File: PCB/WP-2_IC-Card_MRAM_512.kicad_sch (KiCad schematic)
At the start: 18 parts, among them J1 SMS-138-01-G-S, SW1 CUS-14TB, U1 MR2A08xxYSxxx, U2 16827, U3 8T245, U4 MIC5317-3.3YD5, U5 2G32

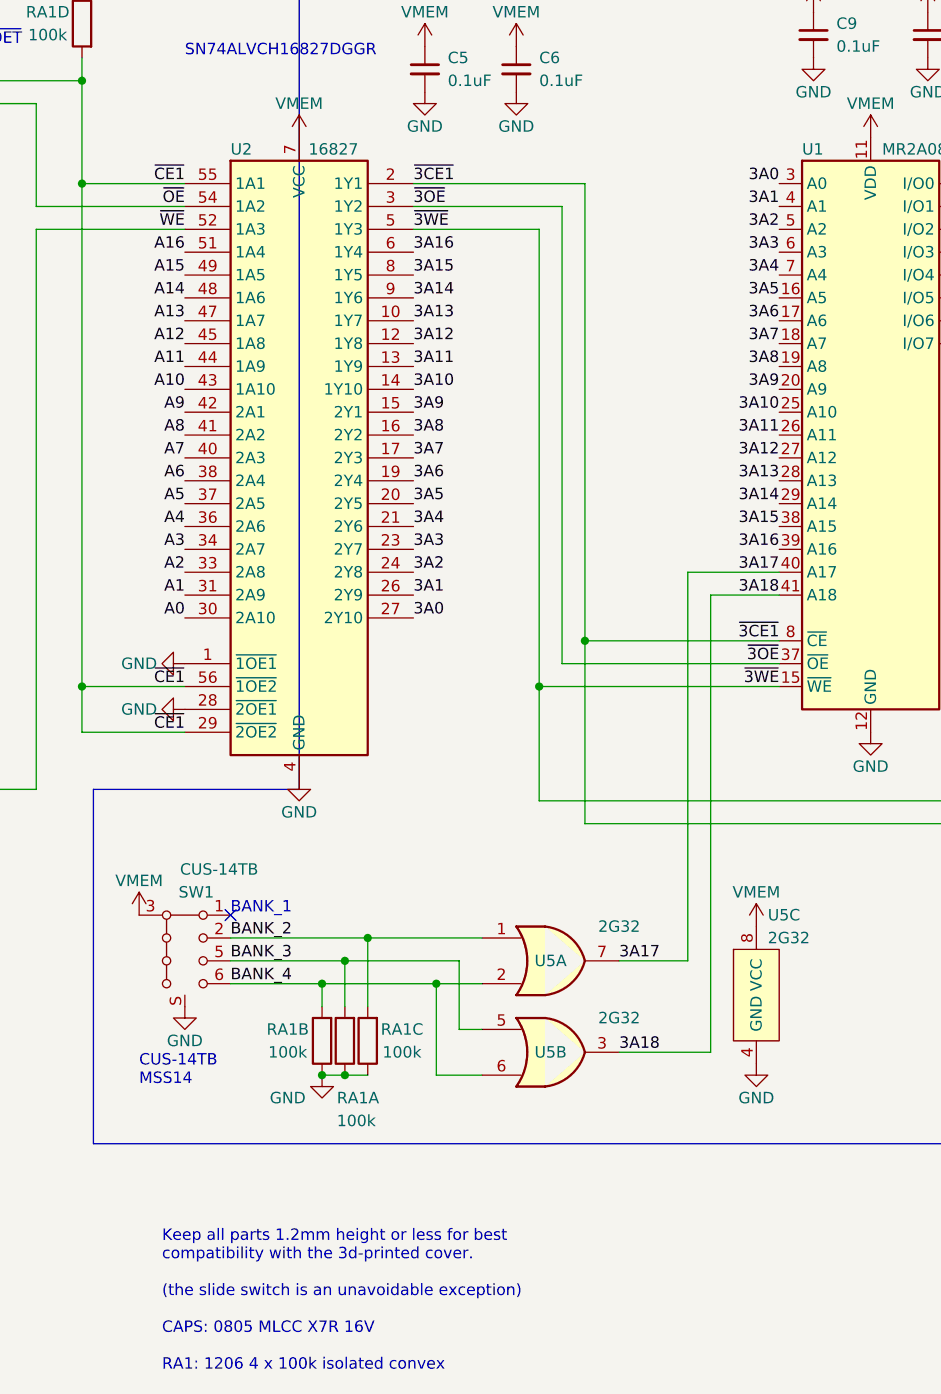
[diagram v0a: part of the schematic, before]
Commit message: mram 512 level-shift parts, battery backed ram top cover
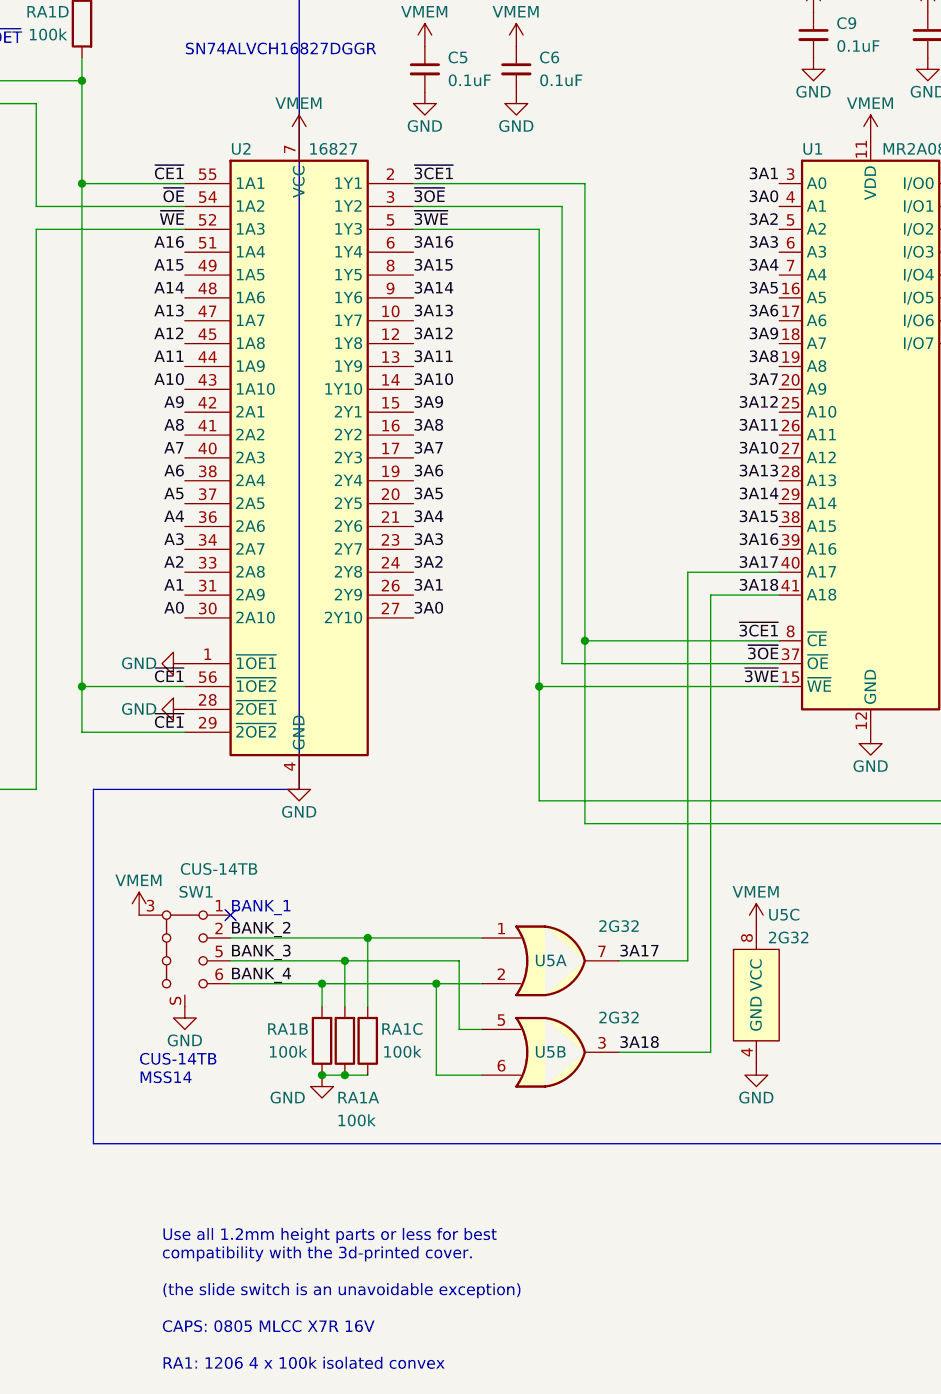
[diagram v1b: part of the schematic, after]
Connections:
- net 3A0: now also U1.4 (A1); no longer U1.3 (A0)
- net 3A1: now also U1.3 (A0); no longer U1.4 (A1)
- net 3A10: now also U1.27 (A12); no longer U1.25 (A10)
- net 3A12: now also U1.25 (A10); no longer U1.27 (A12)
- net 3A7: now also U1.20 (A9); no longer U1.18 (A7)
- net 3A9: now also U1.18 (A7); no longer U1.20 (A9)
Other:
- note added: "Use all 1.2mm height parts or less for best compatibility with the 3d-printed cover. (the slide switch is an unavoidable exception) CAPS: 0805 MLCC X7R 16V RA1: 1206 4 x 100k isolated convex"
- note removed: "Keep all parts 1.2mm height or less for best compatibility with the 3d-printed cover. (the slide switch is an unavoidable exception) CAPS: 0805 MLCC X7R 16V RA1: 1206 4 x 100k isolated convex"
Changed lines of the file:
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@@
     (effects (font (size 1.27 1.27)) (justify left bottom))
   )
-  (text "Keep all parts 1.2mm height or less for best\ncompatibility with the 3d-printed cover.\n\n(the slide switch is an unavoidable exception)\n\nCAPS: 0805 MLCC X7R 16V\n\nRA1: 1206 4 x 100k isolated convex"
+  (text "Use all 1.2mm height parts or less for best\ncompatibility with the 3d-printed cover.\n\n(the slide switch is an unavoidable exception)\n\nCAPS: 0805 MLCC X7R 16V\n\nRA1: 1206 4 x 100k isolated convex"
     (at 99.06 195.58 0)
     (effects (font (size 1.27 1.27)) (justify left bottom))
@@
     (effects (font (size 1.27 1.27)) (justify left bottom))
   )
-  (label "3A0" (at 167.64 63.5 180)
+  (label "3A0" (at 167.64 66.04 180)
     (effects (font (size 1.27 1.27)) (justify right bottom))
   )
@@
     (effects (font (size 1.27 1.27)) (justify left bottom))
   )
-  (label "3A12" (at 167.64 93.98 180)
+  (label "3A12" (at 167.64 88.9 180)
     (effects (font (size 1.27 1.27)) (justify right bottom))
   )
@@
     (effects (font (size 1.27 1.27)) (justify left bottom))
   )
-  (label "3A1" (at 167.64 66.04 180)
+  (label "3A1" (at 167.64 63.5 180)
     (effects (font (size 1.27 1.27)) (justify right bottom))
   )
@@
     (effects (font (size 1.27 1.27)) (justify left bottom))
   )
-  (label "3A7" (at 167.64 81.28 180)
+  (label "3A7" (at 167.64 86.36 180)
     (effects (font (size 1.27 1.27)) (justify right bottom))
   )
@@
     (effects (font (size 1.27 1.27)) (justify left bottom))
   )
-  (label "3A9" (at 167.64 86.36 180)
+  (label "3A9" (at 167.64 81.28 180)
     (effects (font (size 1.27 1.27)) (justify right bottom))
   )
@@
     (effects (font (size 1.27 1.27)) (justify right bottom))
   )
-  (label "3A10" (at 167.64 88.9 180)
-    (effects (font (size 1.27 1.27)) (justify right bottom))
-  )
+  (label "3A10" (at 167.64 93.98 180)
+    (effects (font (size 1.27 1.27)) (justify right bottom))
+  )

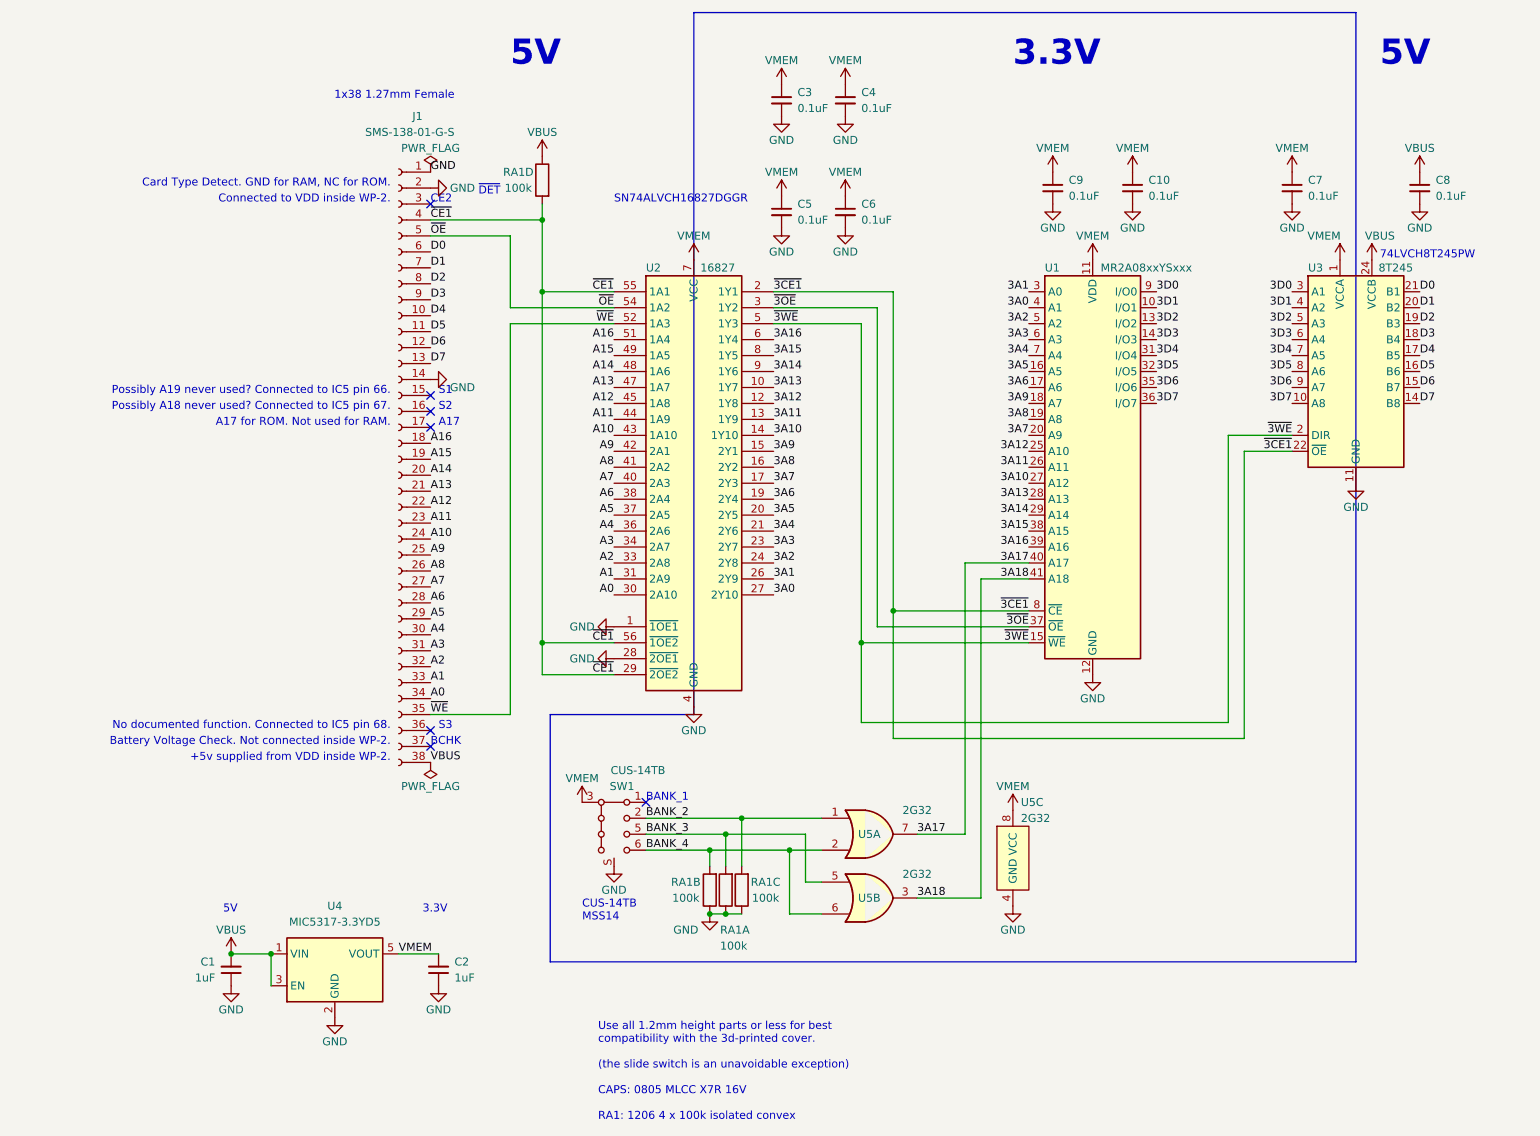
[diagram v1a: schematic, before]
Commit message: MRAM_512 pullups on /3CE1 /3WE
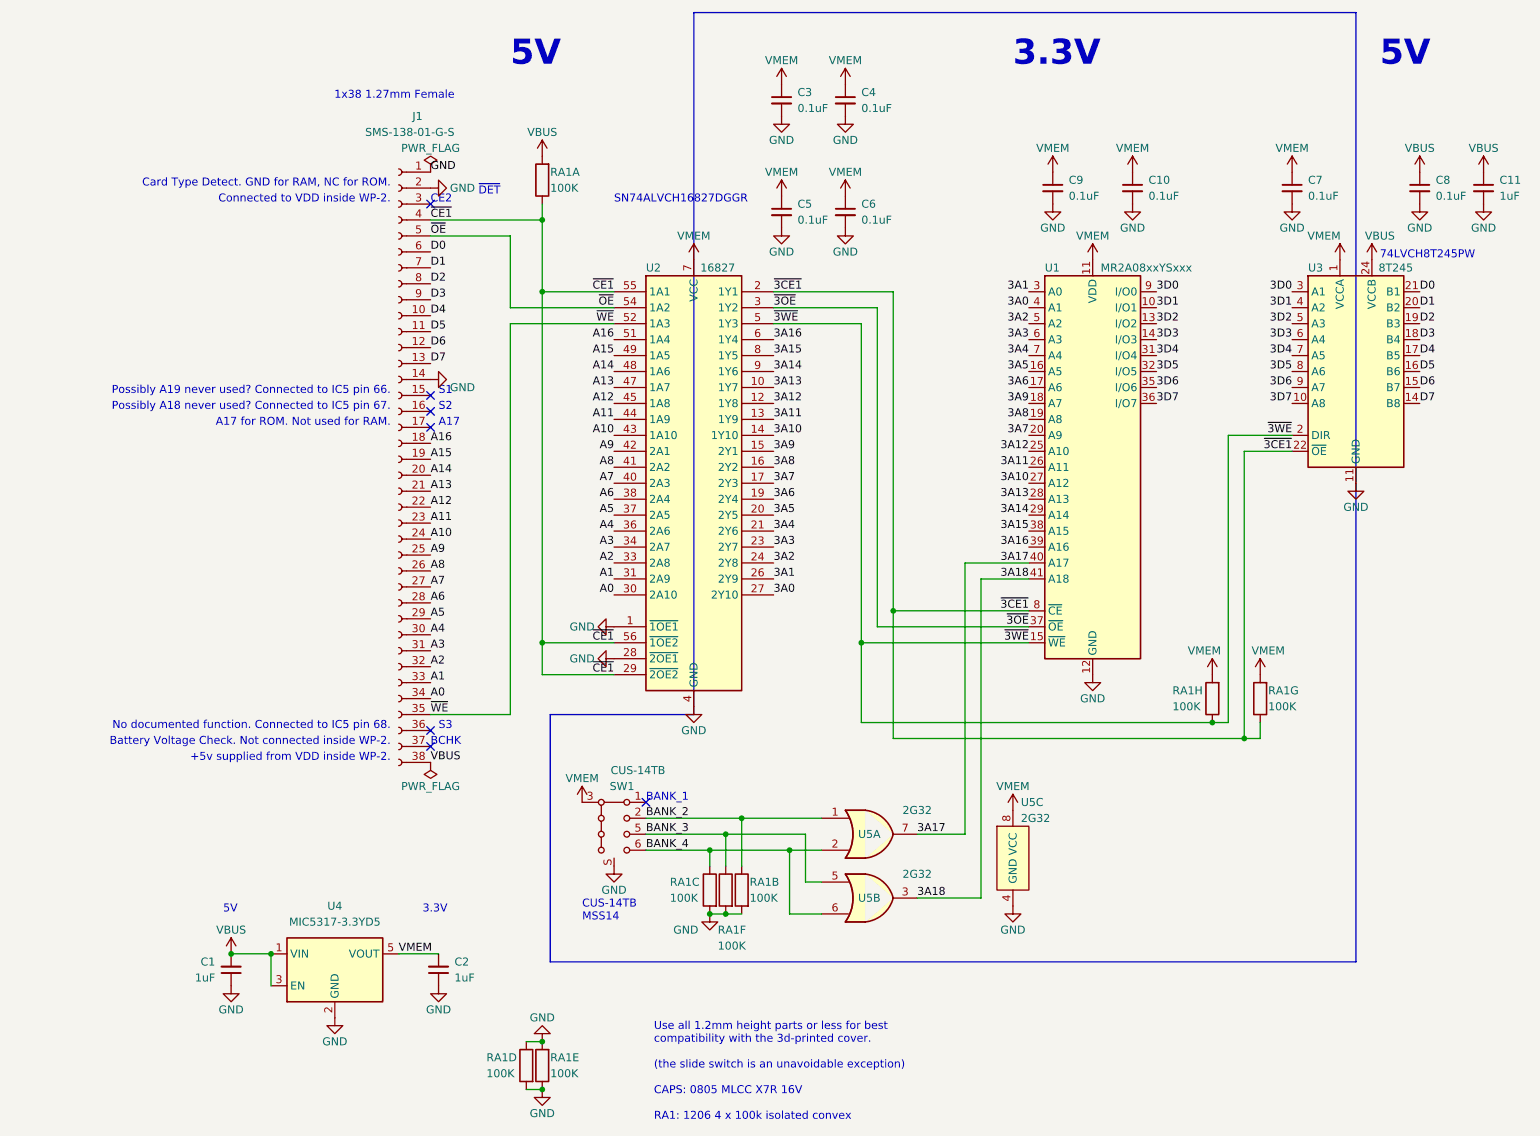
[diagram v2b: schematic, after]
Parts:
- removed RA1: 100k, 0_LOCAL:R_Array_Convex_4x0612, symbol 0_LOCAL:R_Array_04
- added C11: 1uF, 0_LOCAL:C_0805_1mm, symbol 0_LOCAL:C_Small
- added RA1: 100K, 0_LOCAL:R_Array_Convex_8x0602, symbol 0_LOCAL:R_Array_08
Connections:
- net BANK_2: now also RA1.15 (R2.2)
- net BANK_3: now also RA1.11 (R6.2)
- net BANK_4: now also RA1.14 (R3.2)
- net GND: now also C11.2, RA1.12 (R5.2), RA1.13 (R4.2), RA1.2 (R6.1), RA1.3 (R8.1), RA1.4 (R4.1), RA1.5 (R5.1), RA1.6 (R6.1)
- net VBUS: now also C11.1, RA1.1 (R1.1)
- net VMEM: now also RA1.7 (R7.1), RA1.8 (R8.1)
- net ~{3CE1}: now also RA1.10 (R7.2)
- net ~{3WE}: now also RA1.9 (R8.2)
- net ~{CE1}: now also RA1.16 (R1.2)

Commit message: mram 512 pullups & caps & cover
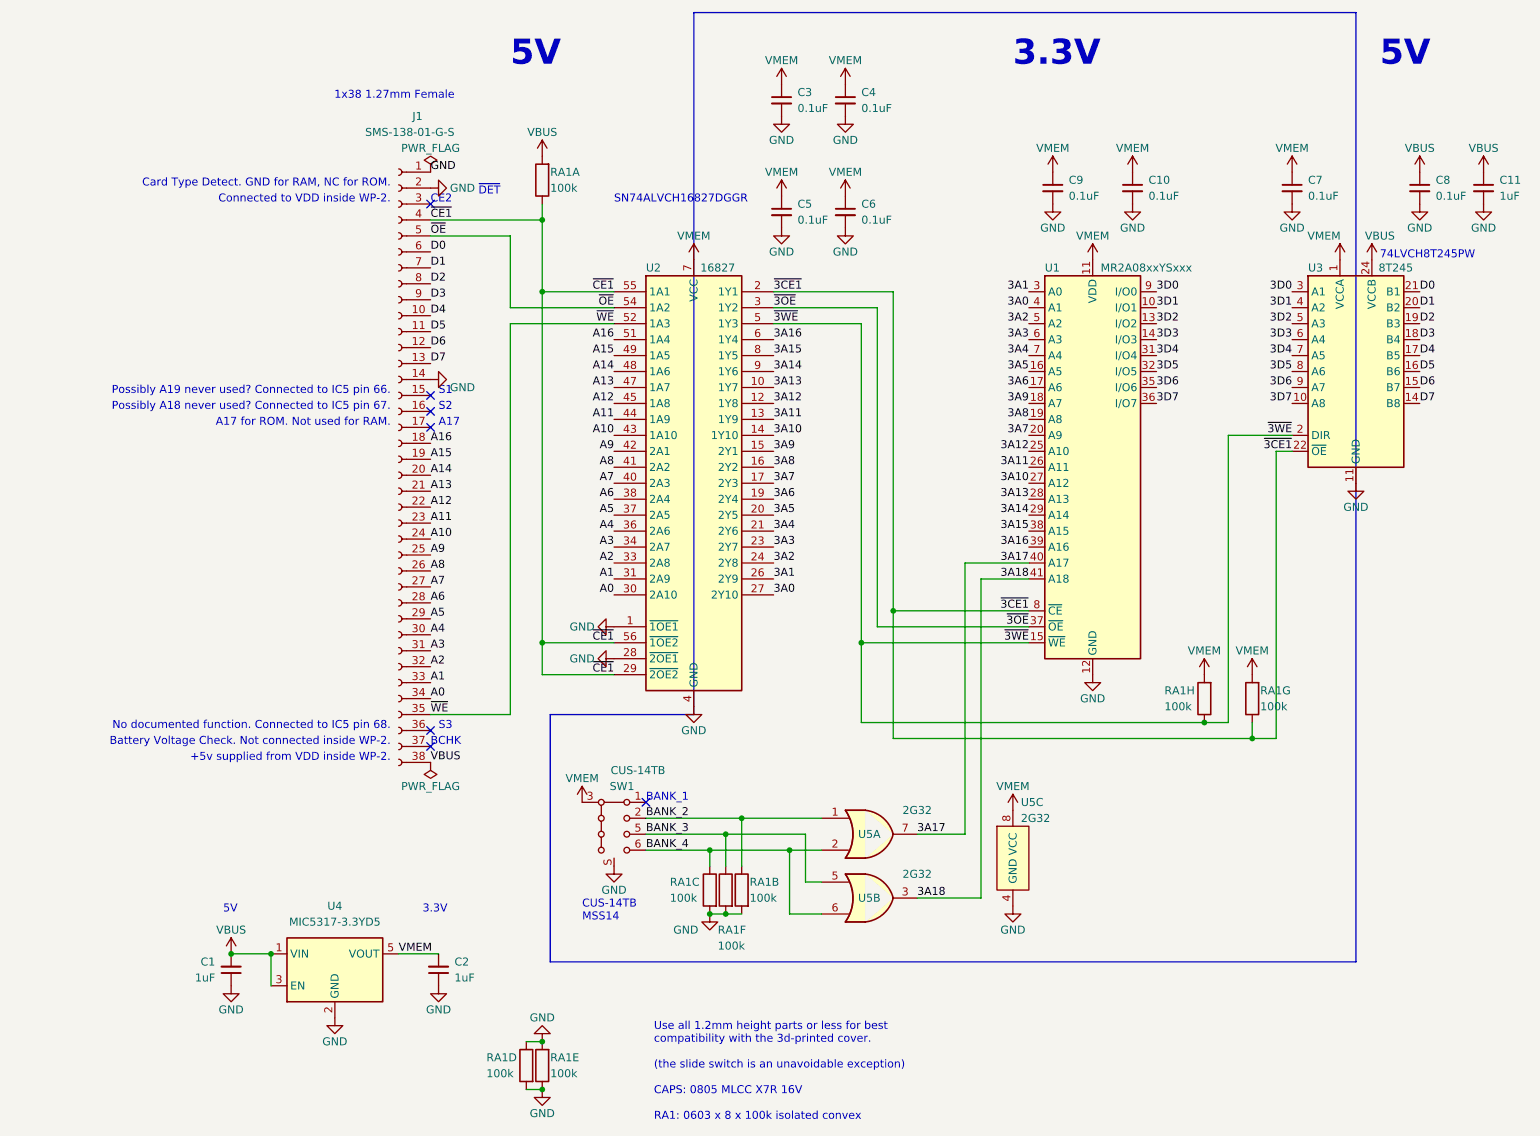
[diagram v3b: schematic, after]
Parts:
- RA1: value 100K -> 100k
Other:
- note added: "Use all 1.2mm height parts or less for best compatibility with the 3d-printed cover. (the slide switch is an unavoidable exception) CAPS: 0805 MLCC X7R 16V RA1: 0603 x 8 x 100k isolated convex"
- note removed: "Use all 1.2mm height parts or less for best compatibility with the 3d-printed cover. (the slide switch is an unavoidable exception) CAPS: 0805 MLCC X7R 16V RA1: 1206 4 x 100k isolated convex"
- moved on the sheet: RA1G, RA1H
